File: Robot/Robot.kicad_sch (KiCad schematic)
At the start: 26 parts, among them J1 Servo1, J10 Lidar, J11 Console, J2 Servo2, J3 Servo3, J4 Servo4, J5 Servo5, J6 Servo6, J7 Servo7, J8 Beacon, J9 DLED, U1 ADC128D818, U2 MaixCAM2

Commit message: Updated PCB for Robot (routing in progress)
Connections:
- net Power/Pwr1: now also J4.2 (Pin_2), J5.2 (Pin_2), J6.2 (Pin_2), J7.2 (Pin_2); no longer J1.2 (Pin_2), J2.2 (Pin_2), J3.2 (Pin_2), J9.1 (Pin_1)
- net Power/Pwr2: now also J1.2 (Pin_2), J2.2 (Pin_2), J3.2 (Pin_2), J9.1 (Pin_1); no longer J4.2 (Pin_2), J5.2 (Pin_2), J6.2 (Pin_2), J7.2 (Pin_2)
- net +3.3V renamed +3V3
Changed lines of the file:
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@@
 	)
 	(symbol
+		(lib_id "power:+3V3")
+		(at 29.21 157.48 270)
+		(unit 1)
+		(exclude_from_sim no)
+		(in_bom yes)
+		(on_board yes)
+		(dnp no)
+		(fields_autoplaced yes)
+		(property "Reference" "#PWR014"
+			(at 25.4 157.48 0)
+			(effects
+				(font
+					(size 1.27 1.27)
+				)
+				(hide yes)
+			)
+		)
+		(property "Value" "+3V3"
+			(at 33.02 157.4799 90)
+			(effects
+				(font
+					(size 1.27 1.27)
+				)
+				(justify left)
+			)
+		)
+		(property "Footprint" ""
+			(at 29.21 157.48 0)
+			(effects
+				(font
+					(size 1.27 1.27)
+				)
+				(hide yes)
+			)
+		)
+		(property "Datasheet" ""
+			(at 29.21 157.48 0)
+			(effects
+				(font
+					(size 1.27 1.27)
+				)
+				(hide yes)
+			)
+		)
+		(property "Description" "Power symbol creates a global label with name \"+3V3\""
+			(at 29.21 157.48 0)
+			(effects
+				(font
+					(size 1.27 1.27)
+				)
+				(hide yes)
+			)
+		)
+		(pin "1"
+		)
+		(instances
+			(project "Robot"
+				(path "/c5aa62e4-5f59-48a4-ae5d-57fc70429dc3"
+					(reference "#PWR014")
+					(unit 1)
+				)
+			)
+		)
+	)
+	(symbol
 		(lib_id "power:GND")
 		(at 115.57 180.34 270)
@@
 	)
 	(symbol
-		(lib_id "power:+3.3V")
-		(at 29.21 157.48 270)
-		(unit 1)
-		(exclude_from_sim no)
-		(in_bom yes)
-		(on_board yes)
-		(dnp no)
-		(fields_autoplaced yes)
-		(property "Reference" "#PWR014"
-			(at 25.4 157.48 0)
-			(effects
-				(font
-					(size 1.27 1.27)
-				)
-				(hide yes)
-			)
-		)
-		(property "Value" "+3.3V"
-			(at 33.02 157.4799 90)
-			(effects
-				(font
-					(size 1.27 1.27)
-				)
-				(justify left)
-			)
-		)
-		(property "Footprint" ""
-			(at 29.21 157.48 0)
-			(effects
-				(font
-					(size 1.27 1.27)
-				)
-				(hide yes)
-			)
-		)
-		(property "Datasheet" ""
-			(at 29.21 157.48 0)
-			(effects
-				(font
-					(size 1.27 1.27)
-				)
-				(hide yes)
-			)
-		)
-		(property "Description" "Power symbol creates a global label with name \"+3.3V\""
-			(at 29.21 157.48 0)
-			(effects
-				(font
-					(size 1.27 1.27)
-				)
-				(hide yes)
-			)
-		)
-		(pin "1"
-		)
-		(instances
-			(project "Robot"
-				(path "/c5aa62e4-5f59-48a4-ae5d-57fc70429dc3"
-					(reference "#PWR014")
-					(unit 1)
-				)
-			)
-		)
-	)
-	(symbol
-		(lib_id "power:+3.3V")
-		(at 115.57 172.72 90)
-		(unit 1)
-		(exclude_from_sim no)
-		(in_bom yes)
-		(on_board yes)
-		(dnp no)
-		(fields_autoplaced yes)
-		(property "Reference" "#PWR015"
-			(at 119.38 172.72 0)
-			(effects
-				(font
-					(size 1.27 1.27)
-				)
-				(hide yes)
-			)
-		)
-		(property "Value" "+3.3V"
-			(at 111.76 172.7199 90)
-			(effects
-				(font
-					(size 1.27 1.27)
-				)
-				(justify left)
-			)
-		)
-		(property "Footprint" ""
-			(at 115.57 172.72 0)
-			(effects
-				(font
-					(size 1.27 1.27)
-				)
-				(hide yes)
-			)
-		)
-		(property "Datasheet" ""
-			(at 115.57 172.72 0)
-			(effects
-				(font
-					(size 1.27 1.27)
-				)
-				(hide yes)
-			)
-		)
-		(property "Description" "Power symbol creates a global label with name \"+3.3V\""
-			(at 115.57 172.72 0)
-			(effects
-				(font
-					(size 1.27 1.27)
-				)
-				(hide yes)
-			)
-		)
-		(pin "1"
-		)
-		(instances
-			(project "Robot"
-				(path "/c5aa62e4-5f59-48a4-ae5d-57fc70429dc3"
-					(reference "#PWR015")
-					(unit 1)
-				)
-			)
-		)
-	)
-	(symbol
 		(lib_id "Connector:Conn_01x03_Pin")
 		(at 251.46 91.44 0)
@@
 	)
 	(symbol
-		(lib_id "power:+3.3V")
-		(at 68.58 29.21 0)
-		(unit 1)
-		(exclude_from_sim no)
-		(in_bom yes)
-		(on_board yes)
-		(dnp no)
-		(fields_autoplaced yes)
-		(property "Reference" "#PWR01"
-			(at 68.58 33.02 0)
-			(effects
-				(font
-					(size 1.27 1.27)
-				)
-				(hide yes)
-			)
-		)
-		(property "Value" "+3.3V"
-			(at 68.58 24.13 0)
-			(effects
-				(font
-					(size 1.27 1.27)
-				)
-			)
-		)
-		(property "Footprint" ""
-			(at 68.58 29.21 0)
-			(effects
-				(font
-					(size 1.27 1.27)
-				)
-				(hide yes)
-			)
-		)
-		(property "Datasheet" ""
-			(at 68.58 29.21 0)
-			(effects
-				(font
-					(size 1.27 1.27)
-				)
-				(hide yes)
-			)
-		)
-		(property "Description" "Power symbol creates a global label with name \"+3.3V\""
-			(at 68.58 29.21 0)
-			(effects
-				(font
-					(size 1.27 1.27)
-				)
-				(hide yes)
-			)
-		)
-		(pin "1"
-		)
-		(instances
-			(project "Robot"
-				(path "/c5aa62e4-5f59-48a4-ae5d-57fc70429dc3"
-					(reference "#PWR01")
-					(unit 1)
-				)
-			)
-		)
-	)
-	(symbol
-		(lib_id "power:+3.3V")
+		(lib_id "power:+3V3")
 		(at 83.82 92.71 270)
 		(unit 1)
@@
 			)
 		)
-		(property "Value" "+3.3V"
-			(at 84.328 89.662 90)
+		(property "Value" "+3V3"
+			(at 84.328 90.17 90)
 			(effects
 				(font
@@
 			)
 		)
-		(property "Description" "Power symbol creates a global label with name \"+3.3V\""
+		(property "Description" "Power symbol creates a global label with name \"+3V3\""
 			(at 83.82 92.71 0)
 			(effects
@@
 	)
 	(symbol
+		(lib_id "power:+3V3")
+		(at 68.58 29.21 0)
+		(unit 1)
+		(exclude_from_sim no)
+		(in_bom yes)
+		(on_board yes)
+		(dnp no)
+		(fields_autoplaced yes)
+		(property "Reference" "#PWR01"
+			(at 68.58 33.02 0)
+			(effects
+				(font
+					(size 1.27 1.27)
+				)
+				(hide yes)
+			)
+		)
+		(property "Value" "+3V3"
+			(at 68.58 24.13 0)
+			(effects
+				(font
+					(size 1.27 1.27)
+				)
+			)
+		)
+		(property "Footprint" ""
+			(at 68.58 29.21 0)
+			(effects
+				(font
+					(size 1.27 1.27)
+				)
+				(hide yes)
+			)
+		)
+		(property "Datasheet" ""
+			(at 68.58 29.21 0)
+			(effects
+				(font
+					(size 1.27 1.27)
+				)
+				(hide yes)
+			)
+		)
+		(property "Description" "Power symbol creates a global label with name \"+3V3\""
+			(at 68.58 29.21 0)
+			(effects
+				(font
+					(size 1.27 1.27)
+				)
+				(hide yes)
+			)
+		)
+		(pin "1"
+		)
+		(instances
+			(project "Robot"
+				(path "/c5aa62e4-5f59-48a4-ae5d-57fc70429dc3"
+					(reference "#PWR01")
+					(unit 1)
+				)
+			)
+		)
+	)
+	(symbol
 		(lib_id "Mechanical:MountingHole")
 		(at 205.74 25.4 0)
@@
 	)
 	(symbol
+		(lib_id "power:+3V3")
+		(at 115.57 172.72 90)
+		(unit 1)
+		(exclude_from_sim no)
+		(in_bom yes)
+		(on_board yes)
+		(dnp no)
+		(fields_autoplaced yes)
+		(property "Reference" "#PWR015"
+			(at 119.38 172.72 0)
+			(effects
+				(font
+					(size 1.27 1.27)
+				)
+				(hide yes)
+			)
+		)
+		(property "Value" "+3V3"
+			(at 111.76 172.7199 90)
+			(effects
+				(font
+					(size 1.27 1.27)
+				)
+				(justify left)
+			)
+		)
+		(property "Footprint" ""
+			(at 115.57 172.72 0)
+			(effects
+				(font
+					(size 1.27 1.27)
+				)
+				(hide yes)
+			)
+		)
+		(property "Datasheet" ""
+			(at 115.57 172.72 0)
+			(effects
+				(font
+					(size 1.27 1.27)
+				)
+				(hide yes)
+			)
+		)
+		(property "Description" "Power symbol creates a global label with name \"+3V3\""
+			(at 115.57 172.72 0)
+			(effects
+				(font
+					(size 1.27 1.27)
+				)
+				(hide yes)
+			)
+		)
+		(pin "1"
+		)
+		(instances
+			(project "Robot"
+				(path "/c5aa62e4-5f59-48a4-ae5d-57fc70429dc3"
+					(reference "#PWR015")
+					(unit 1)
+				)
+			)
+		)
+	)
+	(symbol
 		(lib_id "Connector:Conn_01x03_Pin")
 		(at 215.9 91.44 0)
@@
 		)
 		(pin "Pwr1" output
-			(at 179.07 73.66 0)
+			(at 179.07 69.85 0)
 			(effects
 				(font
@@
 		)
 		(pin "Pwr2" output
-			(at 179.07 69.85 0)
+			(at 179.07 73.66 0)
 			(effects
 				(font

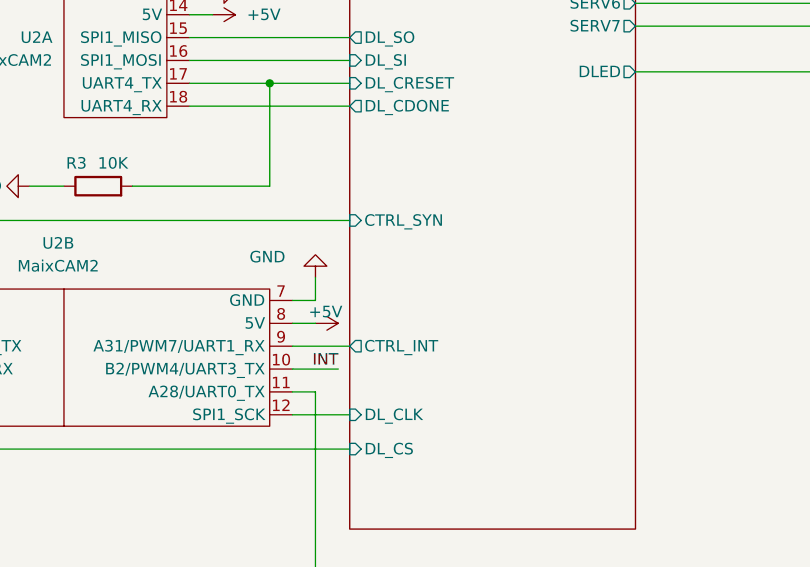
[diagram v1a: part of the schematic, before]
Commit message: Updated PCB for Robot (routing close to finish)
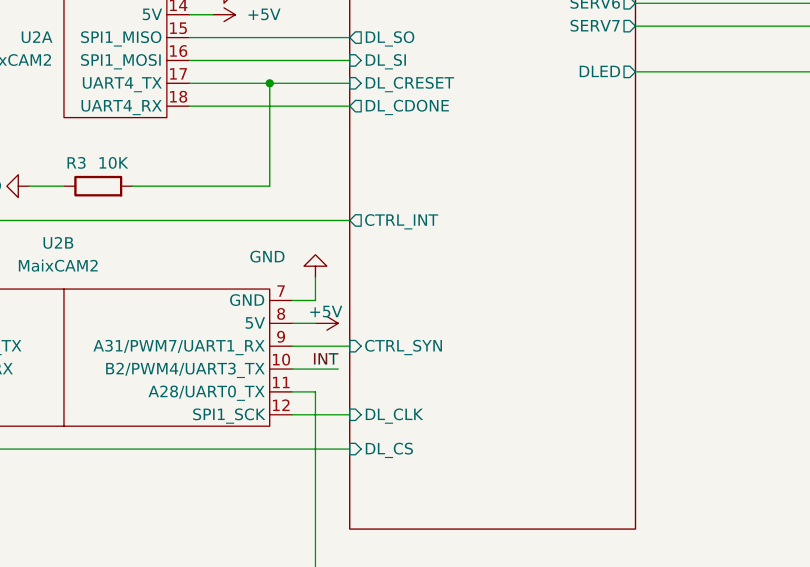
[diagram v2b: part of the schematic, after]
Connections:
- net FPGA/CTRL_INT: now also U2.3 (A30/PWM6/UART1_TX); no longer U2.9 (A31/PWM7/UART1_RX)
- net FPGA/CTRL_SYN: now also U2.9 (A31/PWM7/UART1_RX); no longer U2.3 (A30/PWM6/UART1_TX)
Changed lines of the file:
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@@
 		)
 		(pin "CTRL_INT" output
-			(at 106.68 144.78 180)
+			(at 106.68 130.81 180)
 			(effects
 				(font
@@
 		)
 		(pin "CTRL_SYN" input
-			(at 106.68 130.81 180)
+			(at 106.68 144.78 180)
 			(effects
 				(font
